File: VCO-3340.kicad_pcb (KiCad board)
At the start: 2 copper layers, 80 x 105 mm, 102 parts, among them J10 Conn_01x01, J11 Conn_01x01, J12 Conn_01x01, J13 Conn_01x01, J14 Conn_01x01, J15 Conn_01x01, J16 Conn_01x01, J17 Conn_01x01, J18 Conn_01x01, J19 Conn_01x01, J20 Conn_01x01, J21 Conn_01x01, J22 Conn_01x01, J23 Conn_01x01, J24 Conn_01x01, J6 Conn_01x01, J7 Conn_01x01, J8 Conn_02x05_Odd_Even, J9 Conn_01x01, U1 TL074, U2 AS3340, U3 TL074, U4 LM311, U5 4013, U6 LM79L05_TO92, U7 LM78L05_TO92

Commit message: add labels
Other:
- board text added: "HF"
- board text added: "I Ref"
- board text added: "Saw offset"
- board text added: "Scale"
- board text added: "Sq offset"
- board text added: "Sub offset"
- board text added: "Temp comp"
- board text added: "Tr offs"
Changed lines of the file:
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@@
 		(layer "Edge.Cuts")
+	)
+	(gr_text "Temp comp"
+		(at 137.5 74.5 0)
+		(layer "F.SilkS" knockout)
+		(effects
+			(font
+				(size 1 1)
+				(thickness 0.15)
+			)
+			(justify left bottom)
+		)
+	)
+	(gr_text "Saw offset"
+		(at 150.5 150.5 0)
+		(layer "F.SilkS" knockout)
+		(effects
+			(font
+				(size 1 1)
+				(thickness 0.15)
+			)
+			(justify left bottom)
+		)
+	)
+	(gr_text "HF"
+		(at 155.5 110.5 0)
+		(layer "F.SilkS" knockout)
+		(effects
+			(font
+				(size 1 1)
+				(thickness 0.15)
+			)
+			(justify left bottom)
+		)
+	)
+	(gr_text "Tr offs"
+		(at 156 125.5 0)
+		(layer "F.SilkS" knockout)
+		(effects
+			(font
+				(size 1 1)
+				(thickness 0.15)
+			)
+			(justify left bottom)
+		)
+	)
+	(gr_text "I Ref"
+		(at 185.61 108 0)
+		(layer "F.SilkS" knockout)
+		(effects
+			(font
+				(size 1 1)
+				(thickness 0.15)
+			)
+			(justify left bottom)
+		)
+	)
+	(gr_text "Sub offset"
+		(at 192.5 55.5 0)
+		(layer "F.SilkS" knockout)
+		(effects
+			(font
+				(size 1 1)
+				(thickness 0.15)
+			)
+			(justify left bottom)
+		)
+	)
+	(gr_text "Sq offset"
+		(at 190.5 141 90)
+		(layer "F.SilkS" knockout)
+		(effects
+			(font
+				(size 1 1)
+				(thickness 0.15)
+			)
+			(justify left bottom)
+		)
+	)
+	(gr_text "Scale"
+		(at 205.5 103.5 90)
+		(layer "F.SilkS" knockout)
+		(effects
+			(font
+				(size 1 1)
+				(thickness 0.15)
+			)
+			(justify left bottom)
+		)
 	)
 	(segment

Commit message: small tweaks
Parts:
- C9: value 10p -> 100p
- moved RV8 3.50 mm to (158.0, 110.0)
- moved C5 1.50 mm to (154.0, 98.0)
- moved R37 0.50 mm to (142.4, 110.5)
- moved R38 0.50 mm to (142.4, 114.0)
- moved R39 0.50 mm to (142.4, 117.5)
- moved R40 0.50 mm to (142.4, 121.0)
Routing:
- net /SO: track 44.8 -> 36.1 mm, vias 1 -> 0
- net Net-(U3C--): track 34.3 -> 37.4 mm
- net Net-(U2-VHFT): track 5.75 -> 8.68 mm
- net Net-(U4-+): track 18.4 -> 19.2 mm
- net /HS_IN: track 3.77 -> 4.39 mm
- net Net-(C5-Pad1): track 9.87 -> 9.25 mm
- net Net-(R15-Pad2): track 5.89 -> 6.48 mm
- net Net-(R21-Pad1): vias 1 -> 0
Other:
- board text added: "HF Tr"
- board text removed: "HF"

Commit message: compensation caps
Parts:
- added C22: 100p, Capacitor_THT:C_Disc_D5.1mm_W3.2mm_P5.00mm, F.Cu at (112.0, 64.0)
- added C23: 100p, Capacitor_THT:C_Disc_D5.1mm_W3.2mm_P5.00mm, F.Cu at (130.5, 136.5)
- added C24: 100p, Capacitor_THT:C_Disc_D5.1mm_W3.2mm_P5.00mm, F.Cu at (148.0, 125.0)
- added C25: 100p, Capacitor_THT:C_Disc_D5.1mm_W3.2mm_P5.00mm, F.Cu at (146.5, 135.0)
- added C26: 100p, Capacitor_THT:C_Disc_D5.1mm_W3.2mm_P5.00mm, F.Cu at (146.5, 53.0)
- C9: value 100p -> 22p
- moved RV10 32.9 mm to (125.0, 137.2)
- moved R29 29.3 mm to (151.5, 130.1)
- moved R25 29.0 mm to (126.1, 133.5)
- moved R28 29.0 mm to (126.1, 130.0)
- moved U6 29.0 mm to (122.8, 85.5)
- moved J8 29.0 mm to (179.3, 127.1)
- moved R42 29.0 mm to (116.0, 127.1)
- moved U5 29.0 mm to (164.7, 57.4)
- moved C1 29.0 mm to (158.5, 82.5)
- moved C10 29.0 mm to (178.0, 107.4)
- moved C11 29.0 mm to (169.0, 140.4)
- moved C12 29.0 mm to (146.5, 132.5)
- moved C13 29.0 mm to (130.0, 127.0)
- moved C14 29.0 mm to (146.0, 102.0)
- moved C15 29.0 mm to (142.5, 115.0)
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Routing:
- net Net-(C22-Pad2): track 12.4 -> 25.0 mm
- net Net-(U3B--): track 32.4 -> 20.3 mm
- net -12V: track 316.1 -> 326.1 mm
- net /TR_OUT: track 27.0 -> 34.6 mm
- net Net-(U1B--): track 14.7 -> 18.3 mm
- net Net-(U1C--): track 22.6 -> 26.1 mm
- net Net-(U3A--): track 48.6 -> 45.6 mm
- net /SUB_OUT: track 24.6 -> 27.5 mm
- net Net-(R25-Pad2): track 13.2 -> 10.8 mm
- net /CMP_OUT: track 68.8 -> 71.0 mm
- net +12V: track 258.4 -> 259.9 mm
- net /CV_IN: track 20.6 -> 19.3 mm
- net /FREQ_COARSE: track 23.9 -> 22.7 mm

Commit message: prettier solder pins arrangement
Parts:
- moved J12 30.3 mm to (165.0, 104.5)
- moved J14 15.0 mm to (134.0, 47.5)
- moved J15 15.0 mm to (139.0, 47.5)
- moved J10 5.00 mm to (165.0, 109.5)
- moved J18 5.00 mm to (165.0, 119.5)
- moved J20 5.00 mm to (165.0, 124.5)
- moved J6 5.00 mm to (165.0, 129.5)
- moved J7 5.00 mm to (165.0, 114.5)
- moved C16 2.36 mm to (115.0, 81.6), turned to -90 degrees
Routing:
- net /FREQ_FINE: track 4.42 -> 36.4 mm, vias 0 -> 1
- net /PW_W: track 8.49 -> 22.7 mm
- net /PW_IN: track 7.87 -> 21.2 mm
- net /FM_IN: track 5.04 -> 10.9 mm
- net +5V: track 36.5 -> 41.6 mm
- net /SQ_OUT: track 42.3 -> 38.1 mm
- net -12V: track 326.1 -> 322.6 mm
- net /TR_OUT: track 34.6 -> 32.5 mm

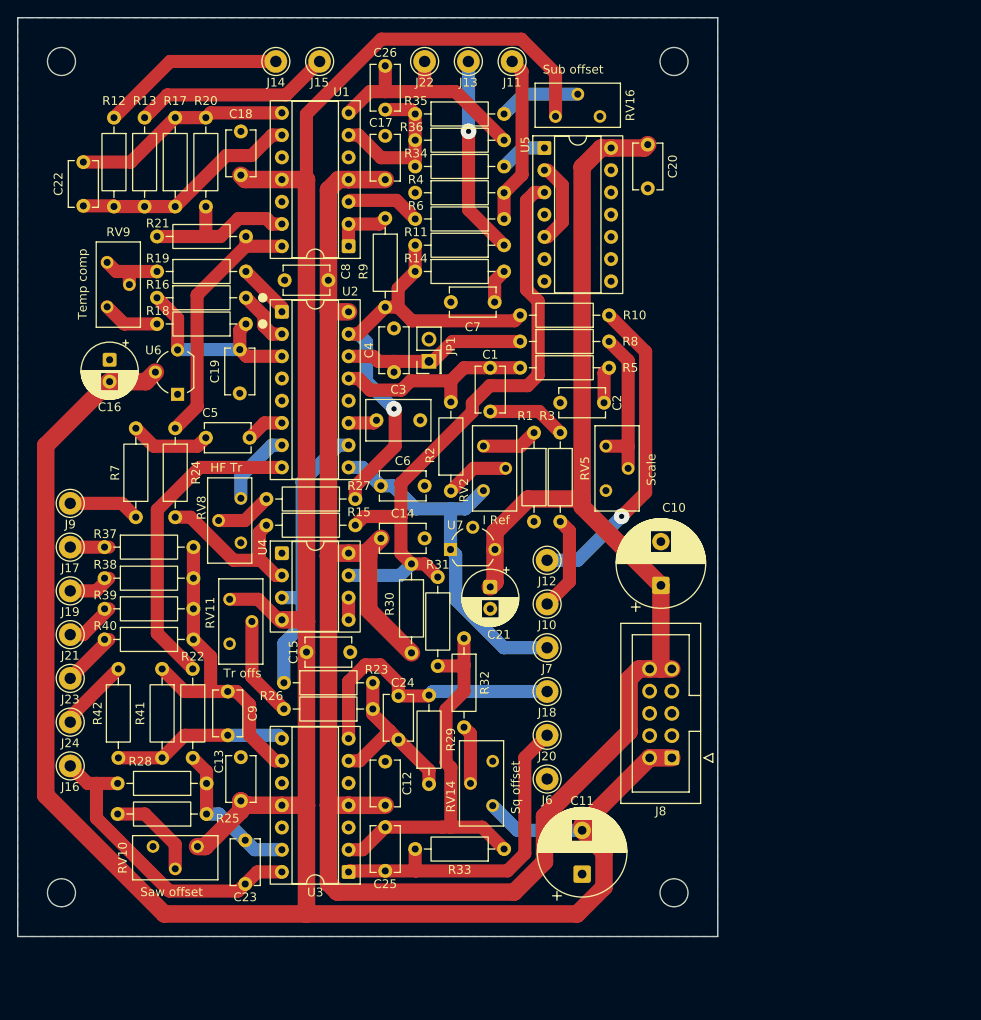
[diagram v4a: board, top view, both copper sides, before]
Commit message: Use 5V regulator to generate offsets
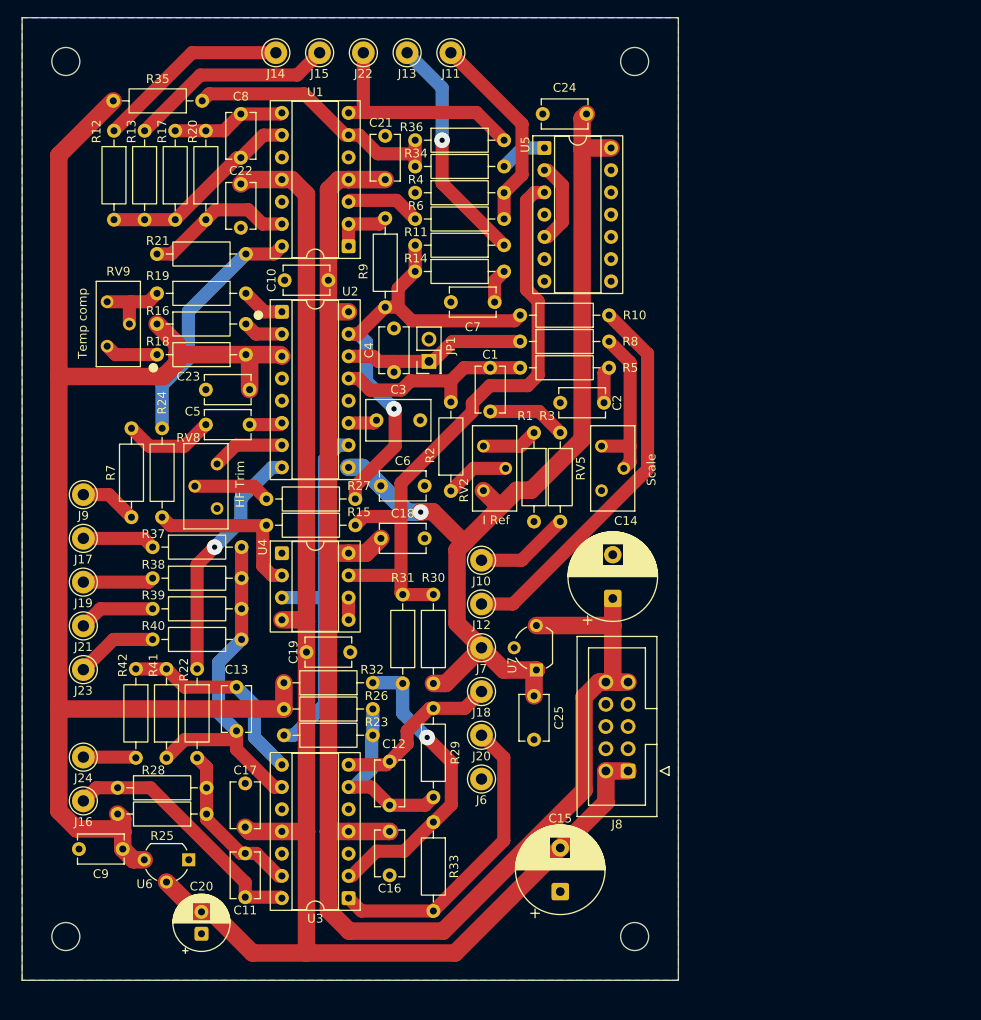
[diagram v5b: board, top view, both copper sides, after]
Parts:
- removed the C21 at (158.5, 107.5)
- removed C26: 100p, Capacitor_THT:C_Disc_D5.1mm_W3.2mm_P5.00mm
- removed RV10, RV11, RV14, RV16: 10k, Potentiometer_THT:Potentiometer_Bourns_3296Y_Vertical
- added C9: 0.1u, Capacitor_THT:C_Disc_D5.1mm_W3.2mm_P5.00mm, F.Cu at (116.5, 137.5)
- C25: value 100p -> 0.1u
- R1: value 22k -> 20k
- R10, R26, R29: value 220k -> 200k
- R23: value 110k -> 100k
- R30: value 4.7k -> 1k
- R31: value 100k -> 18k
- R32: value 100k -> 36k
- R33: value 91k -> 36k
- R34: value 100k -> 10k
- R35: value 100k -> 20k
- R36: value 82k -> 20k
- moved C20 66.4 mm to (125.5, 147.2), turned to 90 degrees
- moved U6 53.2 mm to (124.0, 138.7), turned to 180 degrees
- moved R35 24.4 mm to (125.6, 52.0), turned to 180 degrees
- moved C25 22.7 mm to (163.5, 120.0)
- moved C8 18.8 mm to (130.0, 58.5)
- moved U7 16.9 mm to (163.8, 117.0), turned to 90 degrees
- moved R32 11.6 mm to (145.1, 118.5), turned to 180 degrees
- moved C22 11.0 mm to (130.0, 66.5), turned to 90 degrees
- moved R42 10.4 mm to (118.0, 116.9), turned to -90 degrees
- moved R41 10.2 mm to (121.5, 127.1), turned to 90 degrees
- moved J10 9.01 mm to (157.5, 104.5)
- moved J12 9.01 mm to (157.5, 109.5)
- moved R33 8.65 mm to (152.0, 134.4), turned to -90 degrees
- moved C24 7.83 mm to (169.5, 53.5), turned to 180 degrees
- moved C12 7.57 mm to (147.0, 132.5)
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- renumbered C8 to C10, C23 to C11, C24 to C12, C9 to C13, C10 to C14, C11 to C15, C12 to C16, C13 to C17, C14 to C18, C15 to C19, C16 to C20, C17 to C21, C18 to C22, C19 to C23, C20 to C24, C22 to C8
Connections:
- C24 pad 1: +12V -> +5V
- C25 pad 1: Net-(U3A--) -> +5V
- C25 pad 2: /SQ_OUT -> GND
- R25 pad 2: Net-(R25-Pad2) -> -5V
- R26 pad 2: Net-(R26-Pad2) -> -5V
- R30 pad 2: +12V -> +5V
- R32 pad 2: Net-(R32-Pad2) -> -5V
- R35 pad 2: Net-(R35-Pad2) -> -5V
- U5 pad 14: +12V -> +5V
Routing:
- net -12V: track 322.6 -> 172.0 mm
- net -5V: track 22.4 -> 163.7 mm
- net +12V: track 259.9 -> 177.2 mm
- net +5V: track 41.6 -> 109.8 mm, vias 0 -> 1
- net /TR_OUT: track 32.5 -> 19.5 mm
- net Net-(U1B--): track 18.3 -> 30.5 mm
- net Net-(C8-Pad2): track 25.0 -> 13.0 mm
- net Net-(R26-Pad2): track 11.5 -> 0.00 mm
- net Net-(R25-Pad2): track 10.8 -> 0.00 mm
- net Net-(U3A--): track 45.6 -> 34.9 mm, vias 0 -> 1
- net Net-(R35-Pad2): track 9.36 -> 0.00 mm
- net /TO: track 33.3 -> 42.5 mm
- net /SO: track 36.1 -> 27.7 mm, vias 0 -> 1
- net /FREQ_FINE: track 36.4 -> 44.8 mm, vias 1 -> 0
- net Net-(R32-Pad2): track 6.73 -> 0.00 mm
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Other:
- board size 80 x 105 mm -> 75 x 110 mm
- board text added: "HF Trim"
- board text removed: "HF Tr"
- board text removed: "Saw offset"
- board text removed: "Sq offset"
- board text removed: "Sub offset"
- board text removed: "Tr offs"
